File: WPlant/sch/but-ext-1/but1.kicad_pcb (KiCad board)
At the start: 2 copper layers, 37 x 108 mm, 24 parts, among them J1 Conn_01x02_Pin, J4 But2, J8 MainModule, Q1 SI2301, Q2 Si2302, SW1 SW_Push, SW2 SW_Push, SW3 SW_Push, U1 TS3A44159PWR, U2 SMTSOM365BTR, U3 SMTSOM365BTR

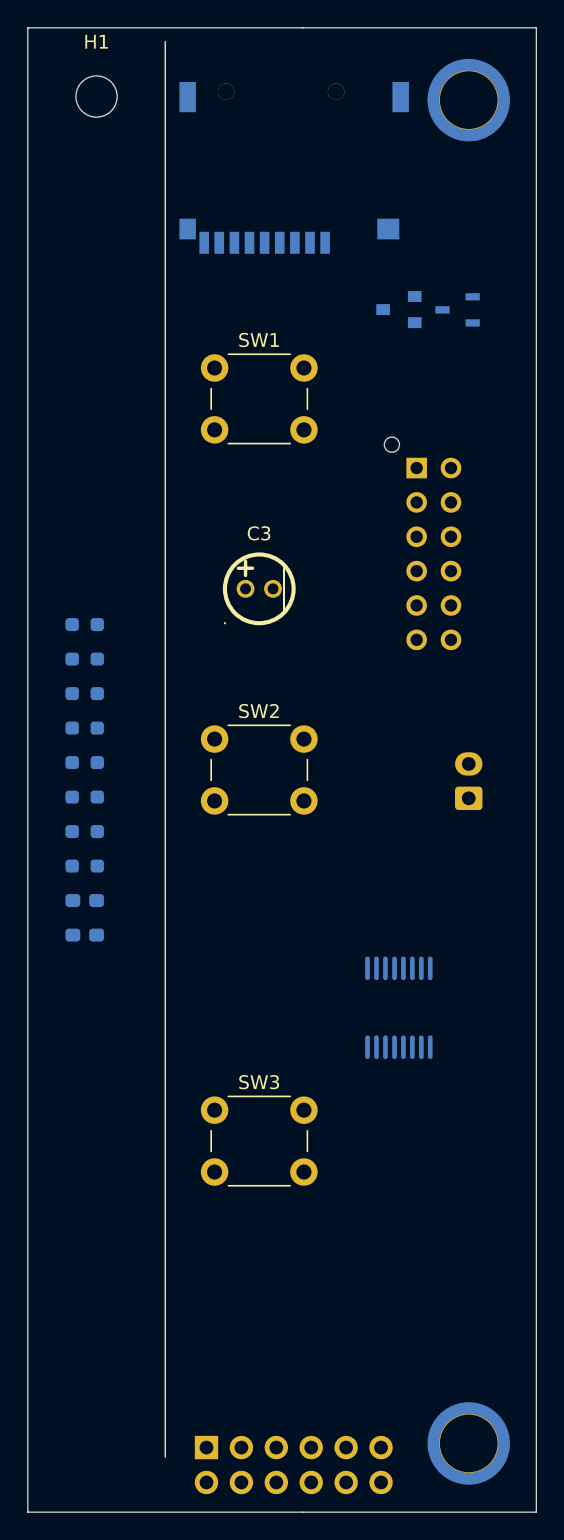
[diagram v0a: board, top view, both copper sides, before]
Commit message: Add 3D model of Robots head pole support
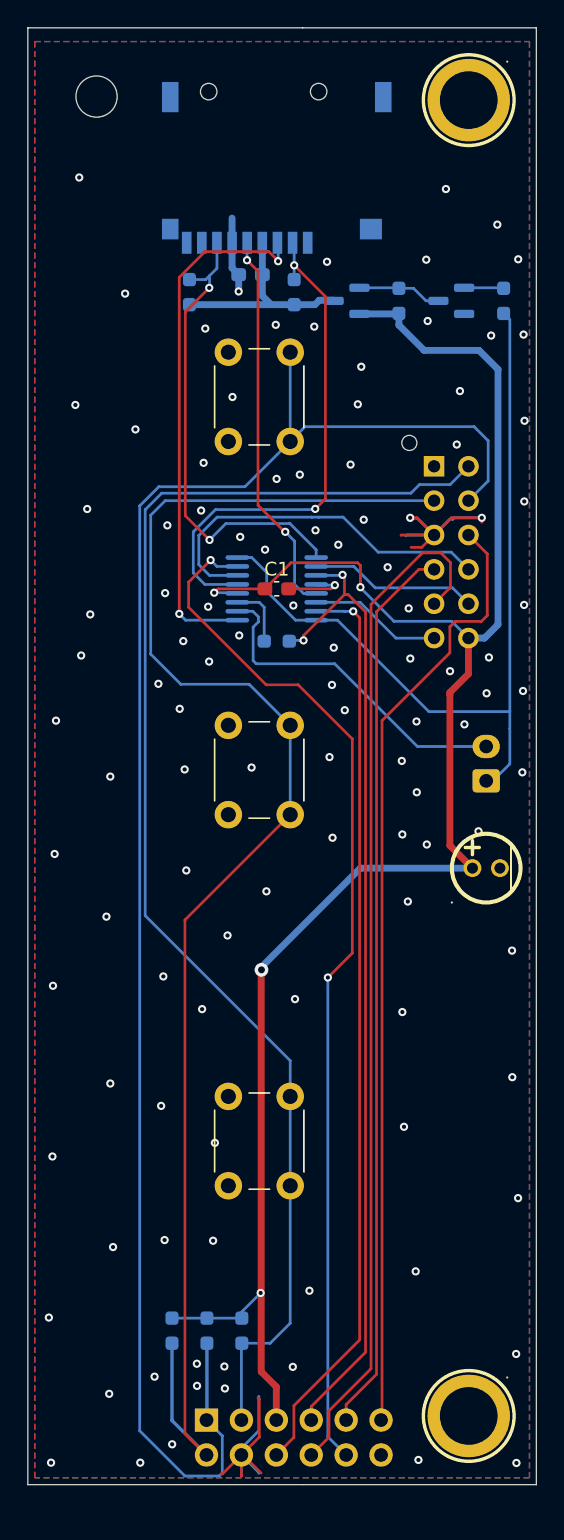
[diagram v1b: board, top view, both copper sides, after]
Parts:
- C1: moved to F.Cu
- Q1: footprint easyeda2kicad:SOT-23-3_L3.0-W1.7-P0.95-LS2.9-BR -> Package_TO_SOT_SMD:SOT-23
- Q2: footprint easyeda2kicad:SOT-23_L2.9-W1.3-P1.90-LS2.4-BR -> Package_TO_SOT_SMD:SOT-23
- U2, U3: footprint easyeda2kicad:SMD_BD5.6-D4.1 -> but:SMD_BD5.6-D4.1; moved to F.Cu
- moved C2 47.1 mm to (116.2, 61.0)
- moved R4 42.9 mm to (115.6, 137.8), turned to 90 degrees
- moved R6 41.8 mm to (134.6, 62.9), turned to -90 degrees
- moved R3 39.3 mm to (110.5, 137.8), turned to 90 degrees
- moved R5 38.6 mm to (127.0, 62.9), turned to -90 degrees
- moved R2 37.4 mm to (113.0, 137.8), turned to 90 degrees
- moved U1 31.8 mm to (118.1, 83.8), turned to -90 degrees
- moved C1 28.8 mm to (118.1, 83.8)
- moved R8 28.6 mm to (119.4, 62.2), turned to 90 degrees
- moved R7 27.8 mm to (111.8, 62.2), turned to 90 degrees
- moved C3 26.2 mm to (133.3, 104.1)
- moved R1 21.5 mm to (118.1, 87.6)
- moved Q1 8.11 mm to (123.2, 62.9), turned to 180 degrees
- moved SW2 5.59 mm to (114.6, 100.2), turned to 90 degrees
- moved SW3 5.59 mm to (114.6, 127.2), turned to 90 degrees
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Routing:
- net +3.3V: track 0.00 -> 135.0 mm, vias 0 -> 4
- net Net-(J4-Pin_1): track 0.00 -> 124.3 mm
- net Net-(J4-Pin_2): track 0.00 -> 109.5 mm
- net Net-(J4-Pin_3): track 0.00 -> 98.1 mm
- net Net-(J4-Pin_10): track 0.00 -> 75.5 mm, vias 0 -> 2
- net /~{eInkReset}: track 0.00 -> 74.8 mm
- net Net-(J4-Pin_7): track 0.00 -> 71.5 mm, vias 0 -> 2
- net /eInkBusy: track 0.00 -> 69.3 mm
- net Net-(J4-Pin_6): track 0.00 -> 66.8 mm, vias 0 -> 1
- net /eInkDC: track 0.00 -> 65.2 mm
- net Net-(J1-Pin_1): track 0.00 -> 60.5 mm
- net GND: track 0.00 -> 47.9 mm, vias 0 -> 111
- net /DI/MOSI: track 0.00 -> 38.5 mm, vias 0 -> 2
- net /CS: track 0.00 -> 37.8 mm, vias 0 -> 2
- net /DO/MISO: track 0.00 -> 34.5 mm, vias 0 -> 2
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- added copper zone on B.Cu, net GND
- added copper zone on F.Cu, net GND
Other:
- board size 37 x 108 mm -> 37 x 106 mm
